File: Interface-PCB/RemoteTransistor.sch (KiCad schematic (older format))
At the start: 25 parts, among them J5 CONN_05JST, J6 CONN_05JST, Q1 2N3904, Q10 2N3904, Q2 2N3904, Q3 2N3904, Q4 2N3904, Q5 2N3904, Q6 2N3904, Q7 2N3904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

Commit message: Assign misc footprints for FDP
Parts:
- U3: footprint digikey-footprints:SOIC-24_W7.50mm -> Package_DIP:DIP-24_W15.24mm_LongPads
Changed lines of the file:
@@
 F 0 "U3" H 4950 6187 60  0000 C CNN
 F 1 "CD74HC4067_MUX" H 4950 6081 60  0000 C CNN
-F 2 "digikey-footprints:SOIC-24_W7.50mm" H 5750 5100 60  0001 L CNN
+F 2 "Package_DIP:DIP-24_W15.24mm_LongPads" H 5750 5100 60  0001 L CNN
 F 3 "http://www.ti.com/general/docs/suppproductinfo.tsp?distId=10&gotoUrl=http%3A%2F%2Fwww.ti.com%2Flit%2Fgpn%2Fcd74hc4067" H 5750 5200 60  0001 L CNN
 F 4 "296-29408-1-ND" H 5750 5300 60  0001 L CNN "Digi-Key_PN"

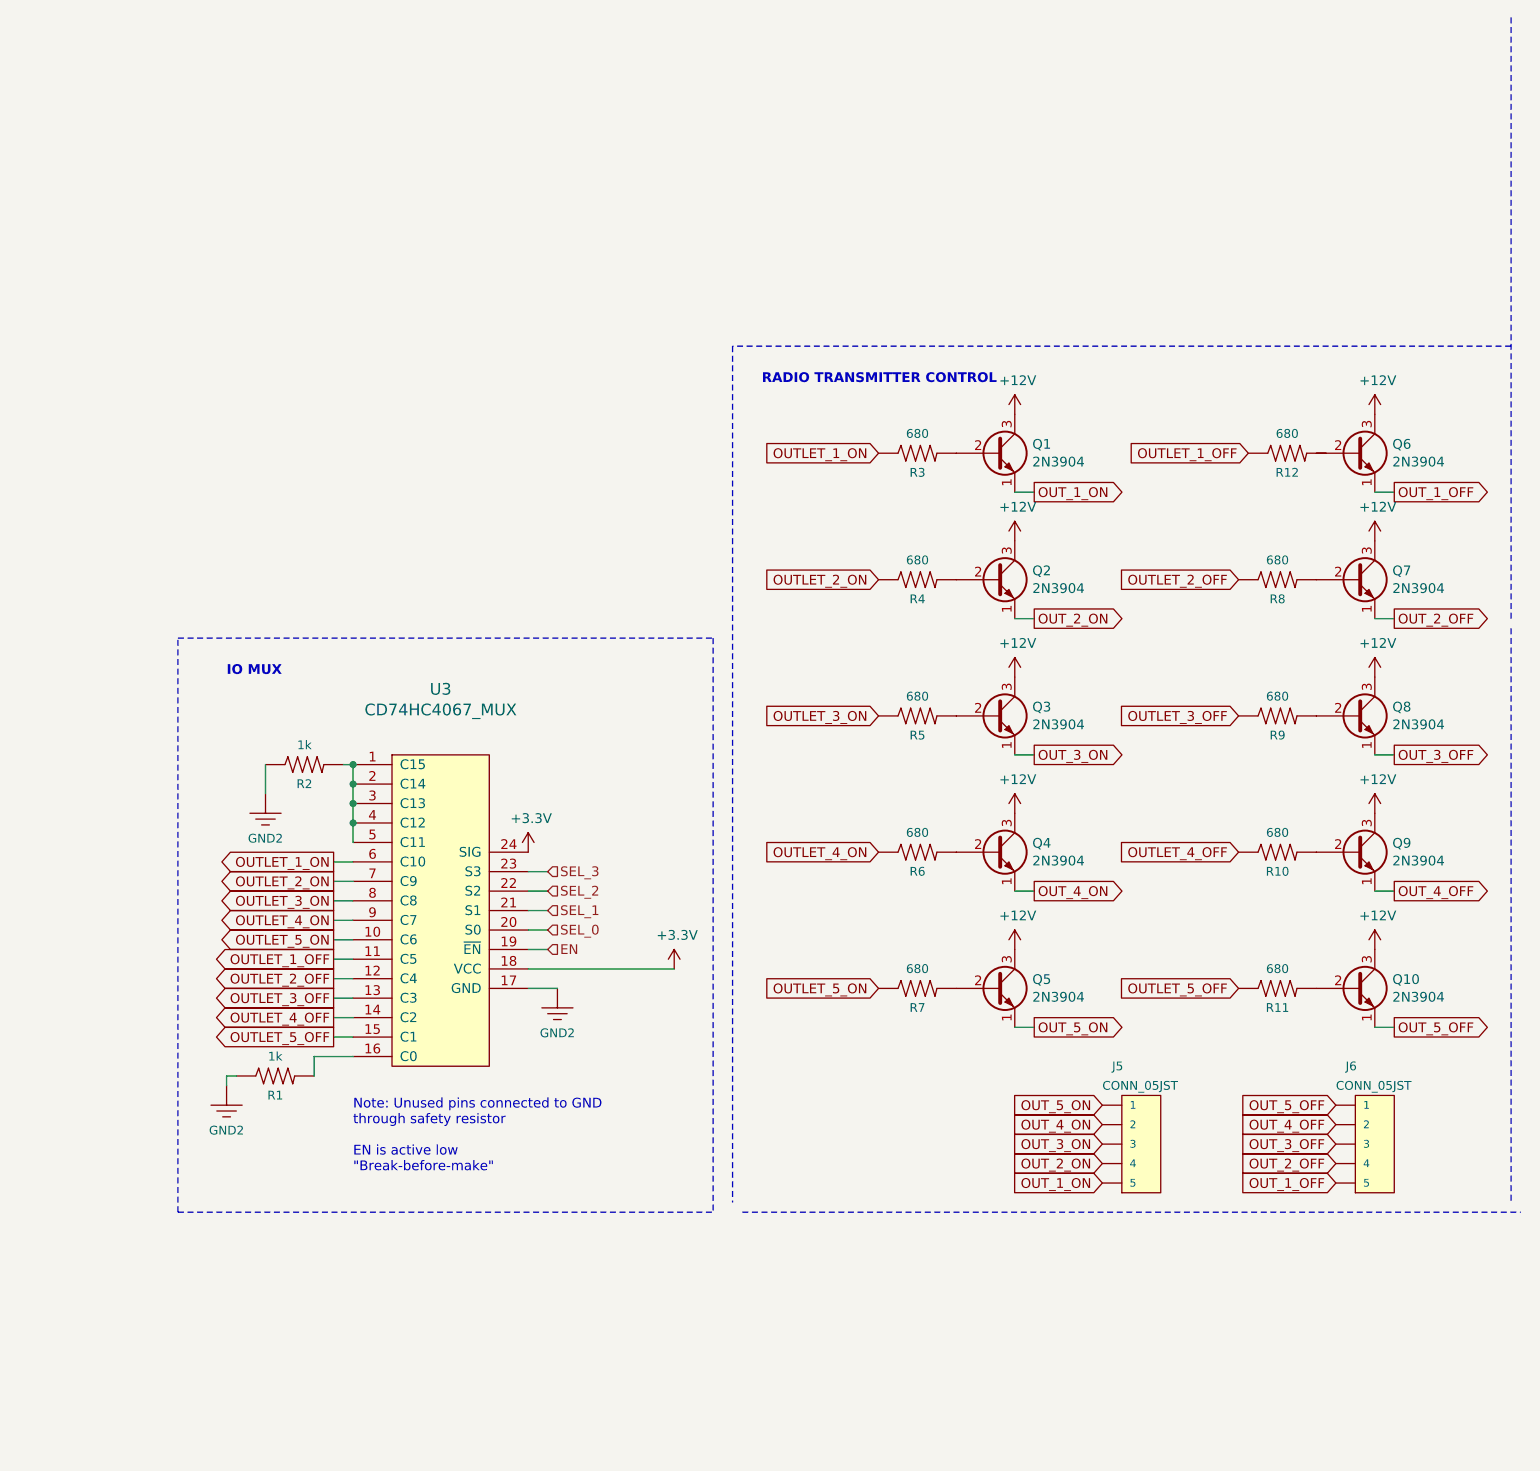
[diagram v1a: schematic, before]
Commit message: Change to Highside switch
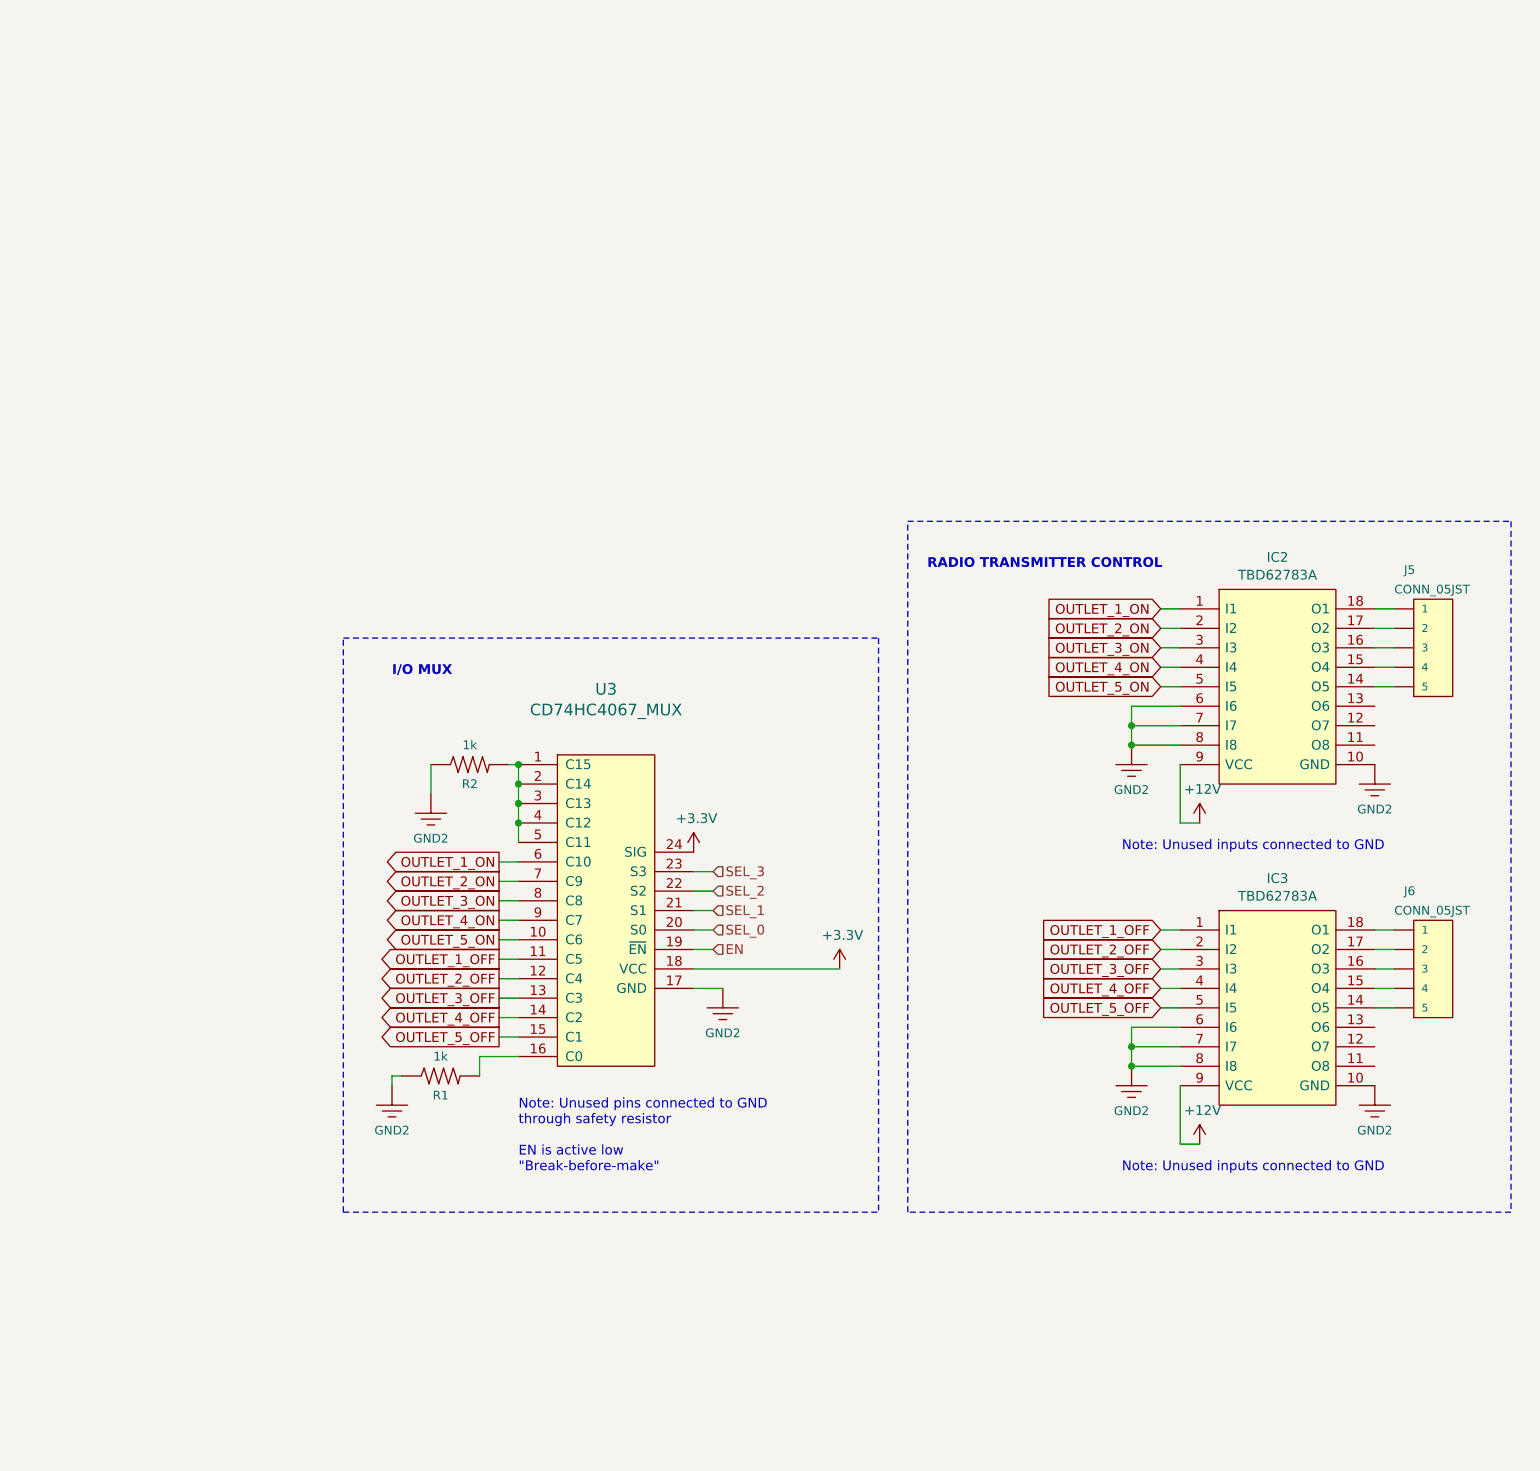
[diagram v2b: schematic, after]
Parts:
- removed Q1, Q10, Q2, Q3, Q4, Q5, Q6, Q7, Q8, Q9: 2N3904, Package_TO_SOT_THT:TO-92_Inline, symbol Transistor_BJT:2N3904
- removed R10, R11, R12, R3, R4, R5, R6, R7, R8, R9: 680, Resistors:AXIAL-0.3-KIT, symbol AA_Custom_Components:R
- added IC2, IC3: TBD62783A, Package_DIP:DIP-18_W7.62mm_LongPads, symbol AA_Custom_Components:TBD62783A
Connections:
- net +12V: now also IC2.9 (VCC), IC3.9 (VCC)
- net 3.3V: now also IC2.10 (GND), IC2.6 (I6), IC2.7 (I7), IC2.8 (I8), IC3.10 (GND), IC3.6 (I6), IC3.7 (I7), IC3.8 (I8)
- net OUTLET_1_OFF: now also IC3.1 (I1)
- net OUTLET_1_ON: now also IC2.1 (I1)
- net OUTLET_2_OFF: now also IC3.2 (I2)
- net OUTLET_2_ON: now also IC2.2 (I2)
- net OUTLET_3_OFF: now also IC3.3 (I3)
- net OUTLET_3_ON: now also IC2.3 (I3)
- net OUTLET_4_OFF: now also IC3.4 (I4)
- net OUTLET_4_ON: now also IC2.4 (I4)
- net OUTLET_5_OFF: now also IC3.5 (I5)
- net OUTLET_5_ON: now also IC2.5 (I5)
- net OUT_1_OFF: no longer names the net of J6.5
- net OUT_1_OFF: now also IC3.14 (O5)
- net OUT_1_ON: no longer names the net of J5.5
- net OUT_1_ON: now also IC2.14 (O5)
- net OUT_2_OFF: no longer names the net of J6.4
- net OUT_2_OFF: now also IC3.15 (O4)
- net OUT_2_ON: no longer names the net of J5.4
- net OUT_2_ON: now also IC2.15 (O4)
- net OUT_3_OFF: no longer names the net of J6.3
- net OUT_3_OFF: now also IC3.16 (O3)
- net OUT_3_ON: no longer names the net of J5.3
- net OUT_3_ON: now also IC2.16 (O3)
- net OUT_4_OFF: no longer names the net of J6.2
- net OUT_4_OFF: now also IC3.17 (O2)
- net OUT_4_ON: no longer names the net of J5.2
- net OUT_4_ON: now also IC2.17 (O2)
- net OUT_5_OFF: no longer names the net of J6.1
- net OUT_5_OFF: now also IC3.18 (O1)
- net OUT_5_ON: no longer names the net of J5.1
- net OUT_5_ON: now also IC2.18 (O1)
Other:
- note added: "I/O MUX"
- note added: "Note: Unused inputs connected to GND"
- note removed: "IO MUX"
- moved on the sheet: J5, R1, R2, U3

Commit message: Add diagrams and datasheets
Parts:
- R1, R2: value 1k -> 10k
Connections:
- no-connect marks 0 -> 6
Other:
- note added: "Note: Inputs have internal 1M Ohm Pulldown. \n Unused inputs connected to GND"
- note added: "Note: Unused pins connected to GND through pulldown (TODO)\n\nEN is active low. All outputs are disconnected when driven high.\n"Break-before-make""
- note removed: "Note: Unused pins connected to GND\nthrough safety resistor\n\nEN is active low\n"Break-before-make""
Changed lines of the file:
@@
 Text GLabel 5250 5500 0    50   Output ~ 0
 OUTLET_2_OFF
-Text GLabel 5250 5800 0    50   Output ~ 0
-OUTLET_5_OFF
 Text GLabel 5250 5700 0    50   Output ~ 0
 OUTLET_4_OFF
@@
 Text Notes 7450 3400 0    50   ~ 10
 RADIO TRANSMITTER CONTROL
-Text GLabel 8650 4000 0    50   Input ~ 0
-OUTLET_5_ON
 Text GLabel 8650 3900 0    50   Input ~ 0
 OUTLET_4_ON
@@
 Wire Wire Line
 	6250 5350 6350 5350
-Text Notes 5350 6500 0    50   ~ 0
-Note: Unused pins connected to GND\nthrough safety resistor\n\nEN is active low\n"Break-before-make"
 Wire Wire Line
 	5250 4900 5350 4900
@@
 P 5100 4400
 F 0 "R2" H 5100 4300 45  0000 C CNN
-F 1 "1k" H 5100 4500 45  0000 C CNN
+F 1 "10k" H 5100 4500 45  0000 C CNN
 F 2 "Resistors:AXIAL-0.3-KIT" H 5100 4550 20  0001 C CNN
 F 3 "" H 5100 4400 60  0001 C CNN
@@
 P 4950 6000
 F 0 "R1" H 4950 5900 45  0000 C CNN
-F 1 "1k" H 4950 6100 45  0000 C CNN
+F 1 "10k" H 4950 6100 45  0000 C CNN
 F 2 "Resistors:AXIAL-0.3-KIT" H 4950 6150 20  0001 C CNN
 F 3 "" H 4950 6000 60  0001 C CNN
@@
 $EndComp
 Wire Wire Line
-	8650 4000 8750 4000
-Wire Wire Line
 	8650 3900 8750 3900
 Wire Wire Line
@@
 Wire Wire Line
 	8750 4400 8750 4700
-$Comp
-L SparkFun-PowerSymbols:GND2 #GND?
-U 1 1 6381AEB8
-P 8500 4300
-AR Path="/6381AEB8" Ref="#GND?"  Part="1"
-AR Path="/6373D3AE/6381AEB8" Ref="#GND0102"  Part="1"
-F 0 "#GND0102" H 8550 4250 45  0001 L BNN
-F 1 "GND2" H 8500 4070 45  0000 C CNN
-F 2 "" H 8500 3975 60  0000 C CNN
-F 3 "" H 8500 4200 60  0001 C CNN
-	1    8500 4300
-	1    0    0    -1
-$EndComp
 Wire Wire Line
 	8750 4100 8500 4100
@@
 Wire Wire Line
 	8750 4300 8500 4300
-Connection ~ 8500 4300
-Text Notes 8450 4850 0    50   ~ 0
-Note: Unused inputs connected to GND
+Text Notes 8400 4900 0    50   ~ 0
+Note: Inputs have internal 1M Ohm Pulldown. \n      Unused inputs connected to GND
 $Comp
 L power:+12V #PWR?
@@
 Wire Notes Line
 	10450 6700 7350 6700
+NoConn ~ 9750 4100
+NoConn ~ 9750 4200
+NoConn ~ 9750 4300
+NoConn ~ 9750 5750
+NoConn ~ 9750 5850
+NoConn ~ 9750 5950
+Text GLabel 5250 5800 0    50   Output ~ 0
+OUTLET_5_OFF
+Wire Wire Line
+	8650 4000 8750 4000
+Connection ~ 8500 4300
+$Comp
+L SparkFun-PowerSymbols:GND2 #GND?
+U 1 1 6381AEB8
+P 8500 4300
+AR Path="/6381AEB8" Ref="#GND?"  Part="1"
+AR Path="/6373D3AE/6381AEB8" Ref="#GND0102"  Part="1"
+F 0 "#GND0102" H 8550 4250 45  0001 L BNN
+F 1 "GND2" H 8500 4070 45  0000 C CNN
+F 2 "" H 8500 3975 60  0000 C CNN
+F 3 "" H 8500 4200 60  0001 C CNN
+	1    8500 4300
+	1    0    0    -1
+$EndComp
+Text GLabel 8650 4000 0    50   Input ~ 0
+OUTLET_5_ON
+Text Notes 4650 6650 0    50   ~ 0
+Note: Unused pins connected to GND through pulldown (TODO)\n\nEN is active low. All outputs are disconnected when driven high.\n"Break-before-make"
 $EndSCHEMATC

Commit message: Review Schematic
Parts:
- added C1, C2: 100nF, Capacitor_THT:C_Disc_D3.4mm_W2.1mm_P2.50mm, symbol Device:C
- added R2, R3, R4, R5: 10k, Resistor_THT:R_Axial_DIN0207_L6.3mm_D2.5mm_P10.16mm_Horizontal, symbol AA_Custom_Components:R
- R1: renamed from R2; footprint Resistors:AXIAL-0.3-KIT -> Resistor_THT:R_Axial_DIN0207_L6.3mm_D2.5mm_P10.16mm_Horizontal
- R6: renamed from R1; footprint Resistors:AXIAL-0.3-KIT -> Resistor_THT:R_Axial_DIN0207_L6.3mm_D2.5mm_P10.16mm_Horizontal
- renumbered IC2 to IC1, IC3 to IC2, J5 to J6, J6 to J7
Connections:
- net +12V: now also C1.1, C2.1
- net at U3.16 (C0): now also R6.P$1 (1); no longer R6.P$2 (2)
- net 3.3V renamed GND
- net GND: now also R1.P$2 (2), R6.P$2 (2), C1.2, C2.2, R2.P$2 (2), R3.P$2 (2), R4.P$2 (2), R5.P$2 (2); no longer R1.P$1 (1), R6.P$1 (1)
- net EN renamed MUX_EN
- net SEL_0 renamed MUX_SEL0
- net SEL_1 renamed MUX_SEL1
- net SEL_2 renamed MUX_SEL2
- net SEL_3 renamed MUX_SEL3
- new net: R1.P$1 (1), U3.1 (C15)
- new net: R2.P$1 (1), U3.2 (C14)
- new net: R3.P$1 (1), U3.3 (C13)
- new net: R4.P$1 (1), U3.4 (C12)
- new net: R5.P$1 (1), U3.5 (C11)
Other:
- moved on the sheet: R1
